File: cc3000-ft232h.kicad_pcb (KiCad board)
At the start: 2 copper layers, 50 x 50 mm, 50 parts, among them CON1 USB-MINI-B, IC1 V_REG_LM1117SOT223, P1 CONN_4X2, P2 CONN_8, P3 CONN_13, P4 CONN_13, P5 CONN_4, P7 CONN_6, U1 U.FL_U.FL, U2 CC3000TEXAS_CC3000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

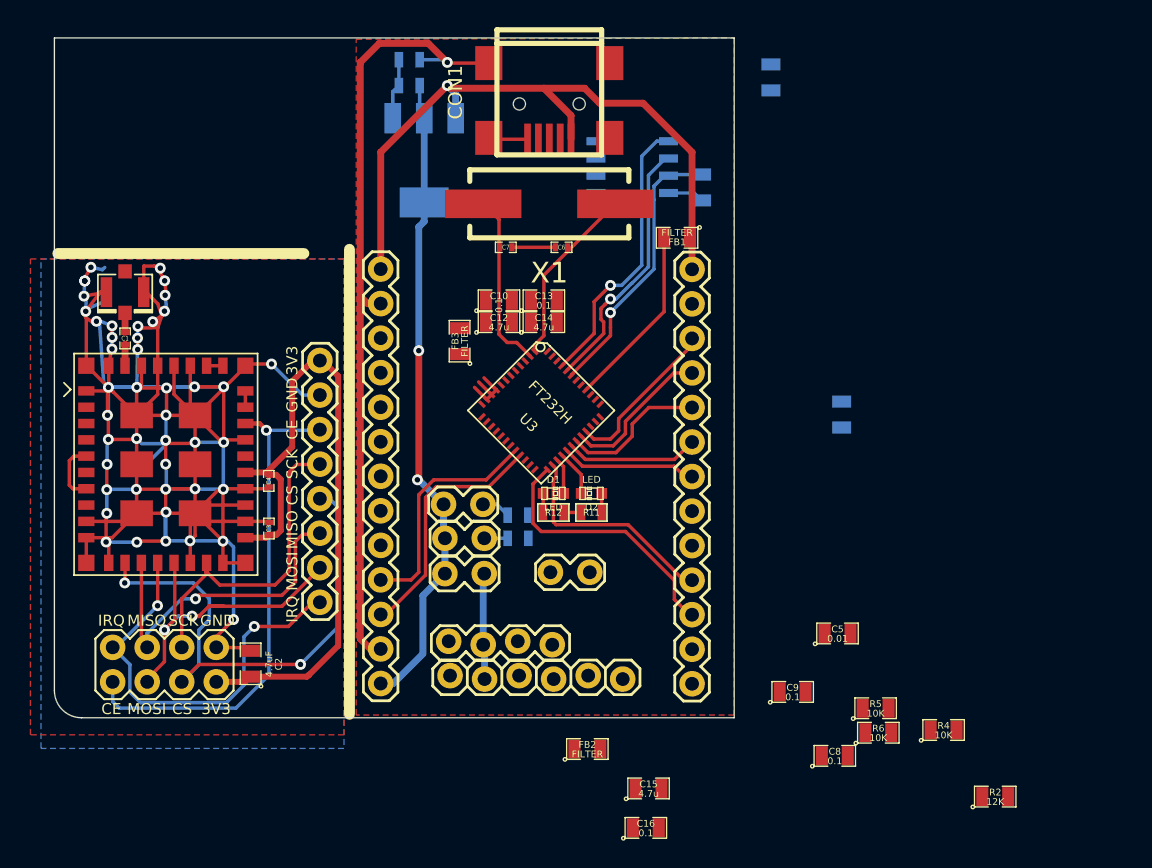
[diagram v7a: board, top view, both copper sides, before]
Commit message: faltam 20 ligaoes e caps mal
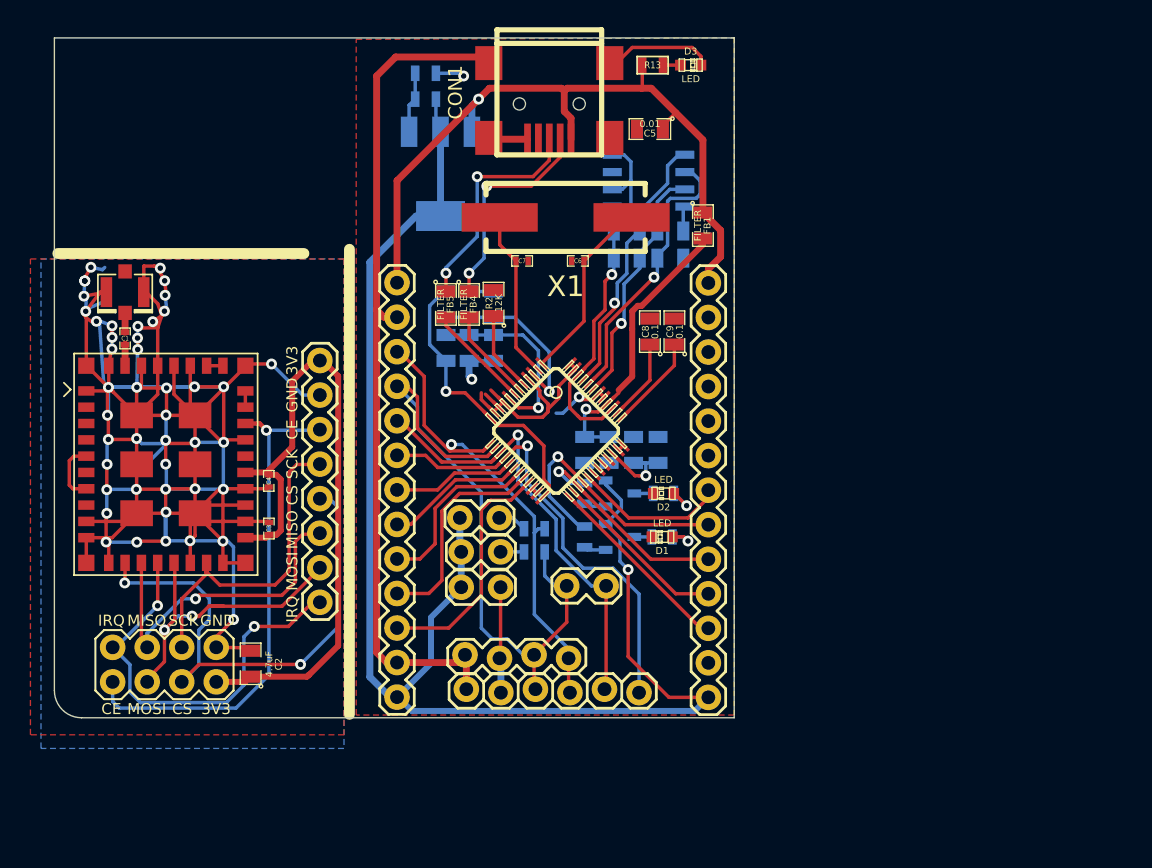
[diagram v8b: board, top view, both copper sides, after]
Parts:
- added D3: LED, LED-0603, F.Cu at (171.8, 72.0)
- added FB4: FILTER, SM0805, F.Cu at (155.5, 89.6)
- added FB5: FILTER, SM0805, F.Cu at (153.8, 89.6)
- added Q1: BCX51, sot23, B.Cu at (166.6, 103.5)
- added Q2: BCX51, sot23, B.Cu at (166.6, 106.7)
- added R13: R, SM0603, F.Cu at (169.0, 72.0)
- added R14: R, SM0603, B.Cu at (164.0, 103.5)
- added R15: R, SM0603, B.Cu at (164.0, 106.7)
- C10, C12, C13, C14, C15, C16, FB2, FB3, R11, R12, R4, R5, R6: moved to B.Cu
- U3: footprint QFN48 -> SparkFun-LQFP-48
- moved R2 51.8 mm to (157.3, 89.5), turned to 90 degrees
- moved R4 41.8 mm to (167.1, 86.2), turned to 180 degrees
- moved R6 41.3 mm to (167.1, 84.2), turned to 180 degrees
- moved C5 39.6 mm to (168.8, 76.7), turned to 180 degrees
- moved R5 36.4 mm to (170.3, 86.2)
- moved FB2 34.3 mm to (153.8, 89.6), turned to 270 degrees
- moved C8 34.0 mm to (168.8, 91.6), turned to 90 degrees
- moved R1 29.2 mm to (167.6, 100.3)
- moved C16 28.2 mm to (164.0, 100.3), turned to 270 degrees
- moved C9 27.9 mm to (170.6, 91.6), turned to 90 degrees
- moved C15 25.1 mm to (165.8, 100.3), turned to 270 degrees
- moved C11 13.7 mm to (169.4, 100.3), turned to 90 degrees
- moved D1 8.62 mm to (169.7, 106.7), turned to 180 degrees
- moved R12 8.20 mm to (169.7, 106.7), turned to 0 degrees
- moved C14 5.65 mm to (155.5, 89.6), turned to 90 degrees
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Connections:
- D1 pad 2: /ft232h/ACBUS3 -> GND
- D2 pad 2: /ft232h/ACBUS4 -> GND
- R11 pad 1: +3.3V -> N-0000044
- R12 pad 1: +3.3V -> N-0000042
- U3 pad 6: /ft232h/USB_D- -> /ft232h/D-
- U3 pad 7: /ft232h/USB_D+ -> /ft232h/D+
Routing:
- net +3.3V: track 100.3 -> 160.5 mm, vias 2 -> 1
- net /ft232h/VCC3V3: track 0.00 -> 48.8 mm, vias 0 -> 2
- net /ft232h/ADBUS1: track 0.00 -> 48.2 mm
- net /ft232h/ADBUS0: track 0.00 -> 35.8 mm, vias 0 -> 1
- net /ft232h/ADBUS2: track 0.00 -> 33.9 mm, vias 0 -> 1
- net GND: track 316.9 -> 350.6 mm, vias 46 -> 48
- net /ft232h/ADBUS3: track 0.00 -> 33.5 mm, vias 0 -> 1
- net /ft232h/USB_D+: track 0.00 -> 16.7 mm, vias 0 -> 2
- net /ft232h/ACBUS4: track 3.40 -> 20.0 mm, vias 0 -> 1
- net /ft232h/USB_D-: track 0.00 -> 15.9 mm, vias 0 -> 2
- net N-0000053: track 0.00 -> 14.0 mm, vias 0 -> 1
- net N-0000060: track 0.00 -> 13.4 mm, vias 0 -> 1
- net /ft232h/ACBUS3: track 2.66 -> 16.0 mm, vias 0 -> 1
- net /ft232h/ADBUS6: track 0.00 -> 13.0 mm
- net /ft232h/ACBUS9: track 11.9 -> 0.00 mm
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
